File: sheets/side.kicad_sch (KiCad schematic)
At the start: 51 parts, among them J1 Battery, SW1 SW_Push, SW11 SW_Push, SW12 SW_Push, SW13 SW_Push, SW14 SW_Push, SW15 SW_Push, SW21 SW_Push, SW22 SW_Push, SW23 SW_Push, SW24 SW_Push, SW25 SW_Push, SW3 SW_Push, SW31 SW_Push, SW32 SW_Push, SW33 SW_Push, SW34 SW_Push, SW35 SW_Push, SW41 SW_Push, SW43 SW_Push, SW5 SW_Push, SW7 SW_Push, SW9 SW_Push, U1 nice_nano

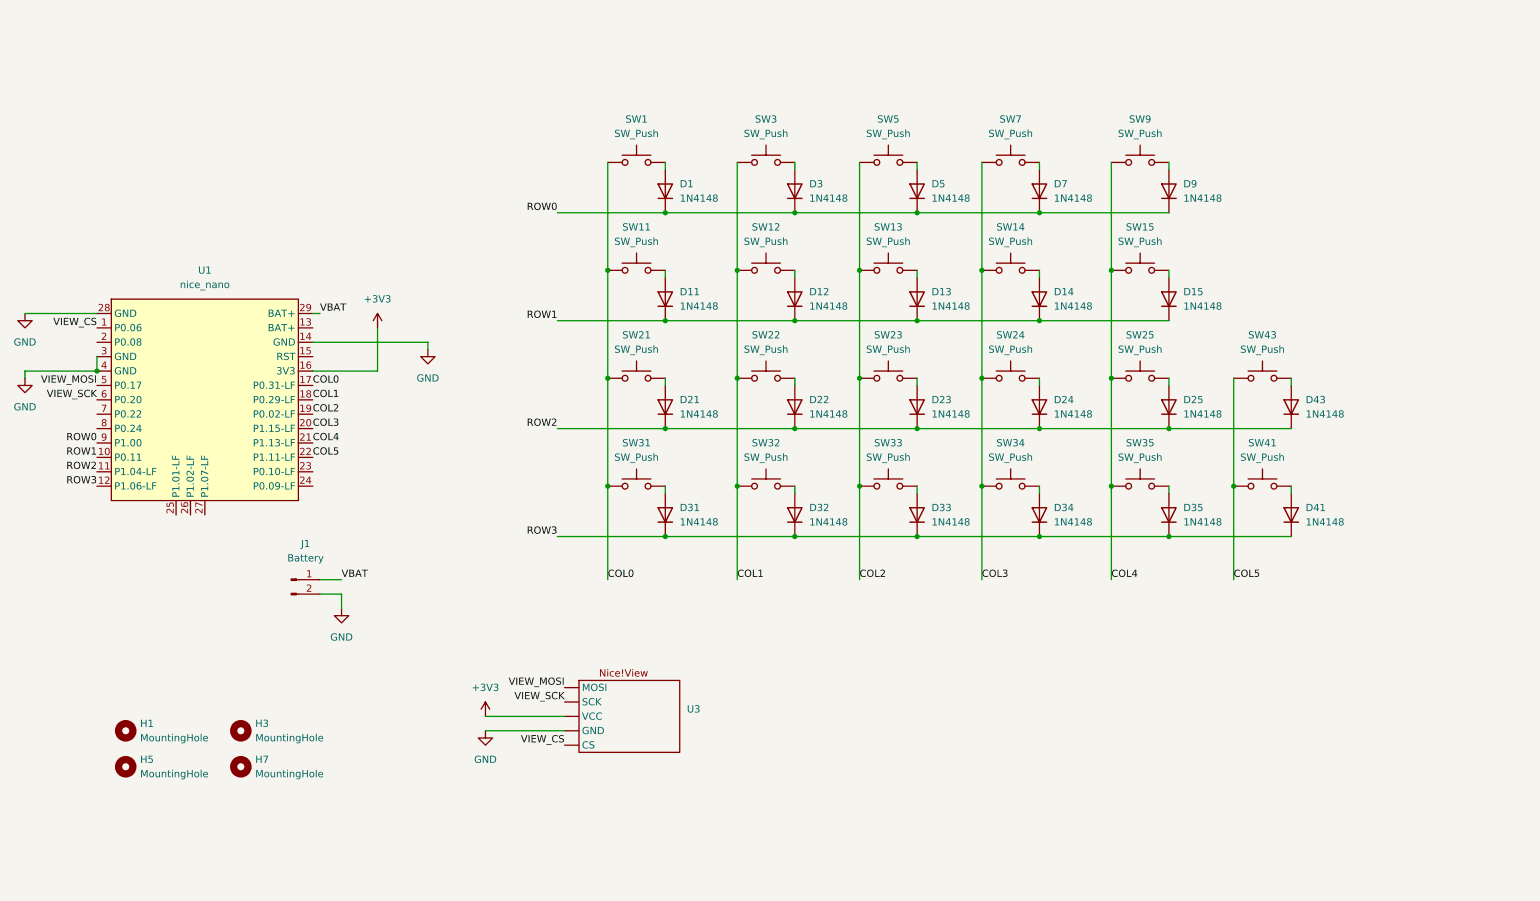
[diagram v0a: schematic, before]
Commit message: add LEDs
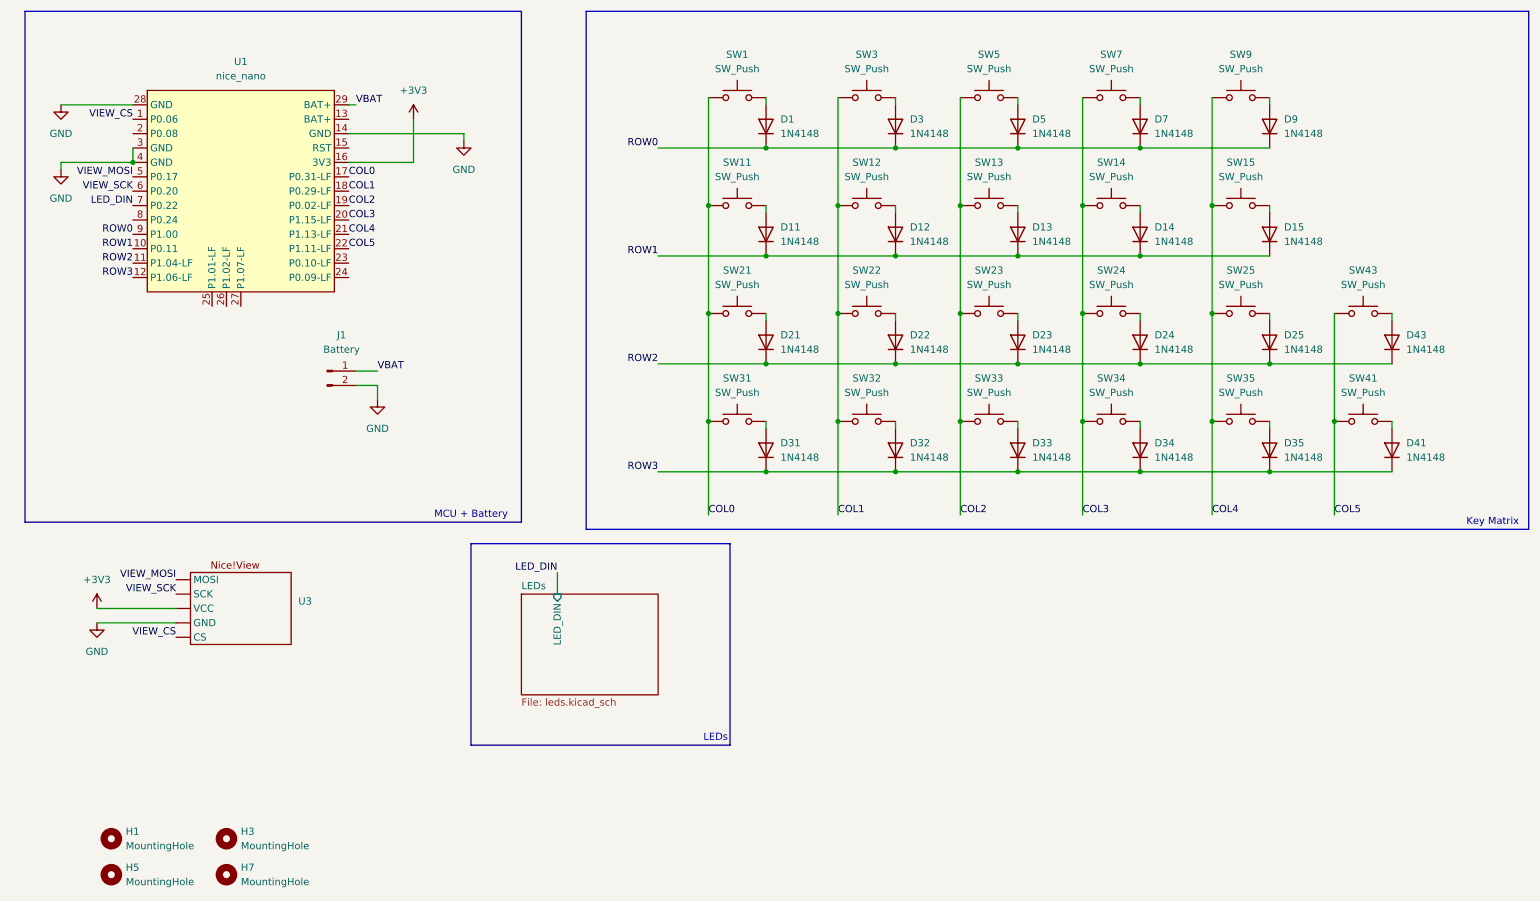
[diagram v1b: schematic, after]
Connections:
- net LED_DIN: now reaches U1.7 (P0.22)
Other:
- added sheet LEDs (leds.kicad_sch)
- note added: "Key Matrix"
- note added: "LEDs"
- note added: "MCU + Battery"
- moved on the sheet: D1, D11, D12, D13, D14, D15, D21, D22, D23, D24, D25, D3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
